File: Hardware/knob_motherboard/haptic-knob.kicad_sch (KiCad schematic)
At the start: 0 parts

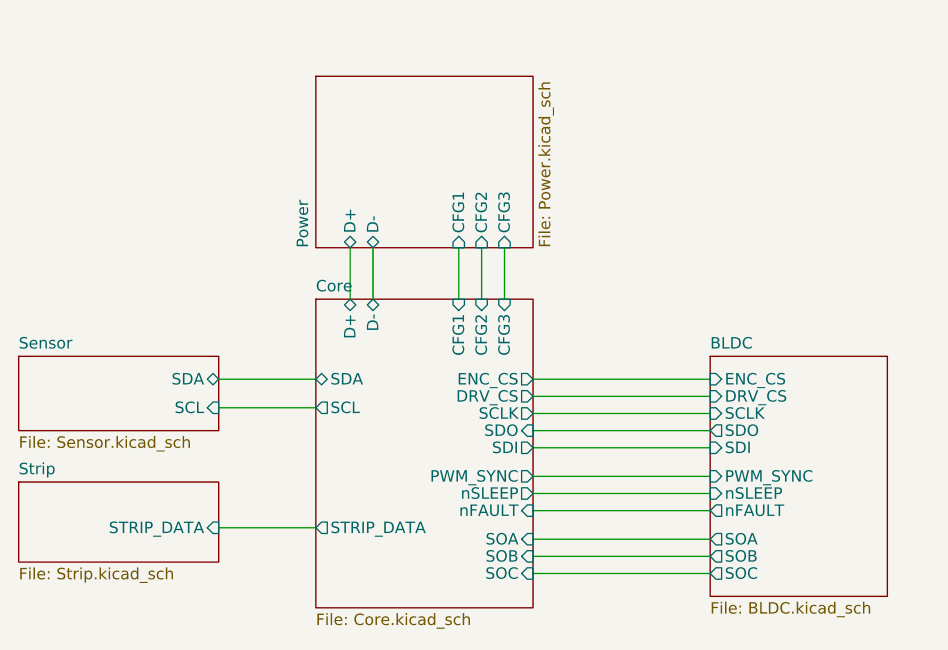
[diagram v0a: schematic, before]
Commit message: drv8311 spi bugfix & ch224k CFG1 bugfix
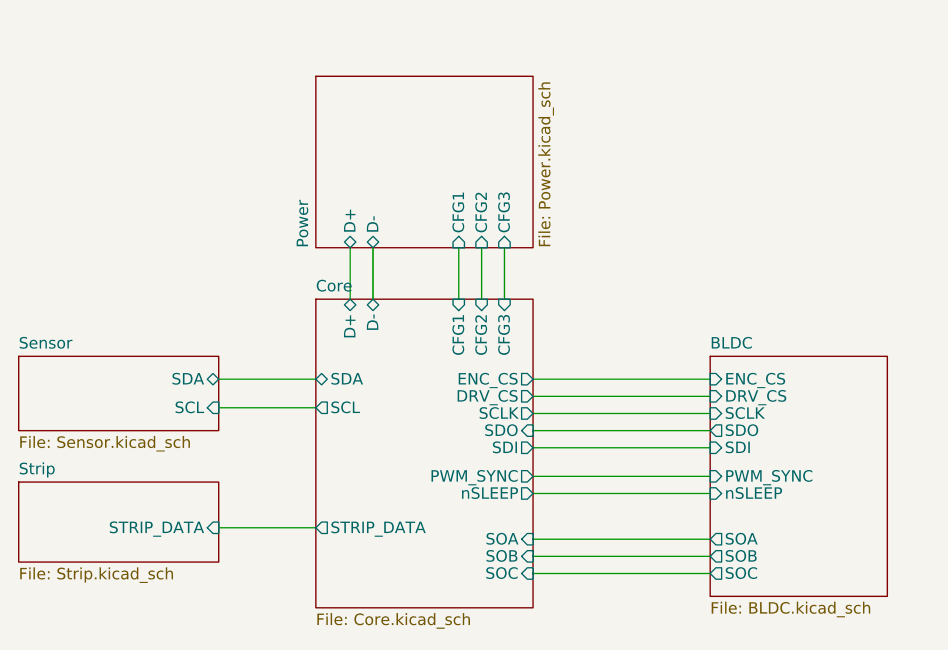
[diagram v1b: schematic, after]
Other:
- sheet BLDC ports: added none; removed nFAULT
- sheet Core ports: added none; removed nFAULT
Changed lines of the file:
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@@
-    (stroke (width 0) (type default))
-  )
-  (wire (pts (xy 137.795 102.235) (xy 157.48 102.235))
     (stroke (width 0) (type default))
   )
@@
       (effects (font (size 1.27 1.27)) (justify left))
     )
-    (pin "nFAULT" output (at 157.48 102.235 180)
-      (effects (font (size 1.27 1.27)) (justify left))
-    )
     (pin "DRV_CS" input (at 157.48 89.535 180)
       (effects (font (size 1.27 1.27)) (justify left))
@@
       (effects (font (size 1.27 1.27)) (justify right))
     )
-    (pin "nFAULT" input (at 137.795 102.235 0)
-      (effects (font (size 1.27 1.27)) (justify right))
-    )
